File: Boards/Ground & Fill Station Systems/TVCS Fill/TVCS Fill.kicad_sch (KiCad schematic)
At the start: 111 parts, among them IC1 NSVT30010MXV6T1G, IC2 NSVT30010MXV6T1G, IC3 ADS1115IRUGR, J1 Conn_01x01_Socket, J10 Conn_01x01_Socket, J11 Conn_01x01_Socket, J12 Conn_01x01_Socket, J13 1190298, J14 1190298, J15 Conn_01x01_Socket, J17 XT30UPB-M, J18 Conn_01x01_Socket, J19 Conn_01x01_Socket, J2 1190297, J3 XT30UPB-M, J4 XT30UPB-M, J5 1190298, J6 XT30UPB-M, J8 Conn_01x01_Socket, J9 Conn_01x01_Socket, Q1 2N7002H6327XTSA2, U1 MAX31856MUD+T, U10 MAX31856MUD+T, U11 IRLZ44NPBF, U12 IRLZ44NPBF, U13 LM61460AASQRJRRQ1, U16 IRLZ44NPBF, U17 MAX485CSA+T, U3 MAX31856MUD+T, U4 PCA9306DP_118, U5 MCP9808T-E/MC, U9 LM61460AASQRJRRQ1

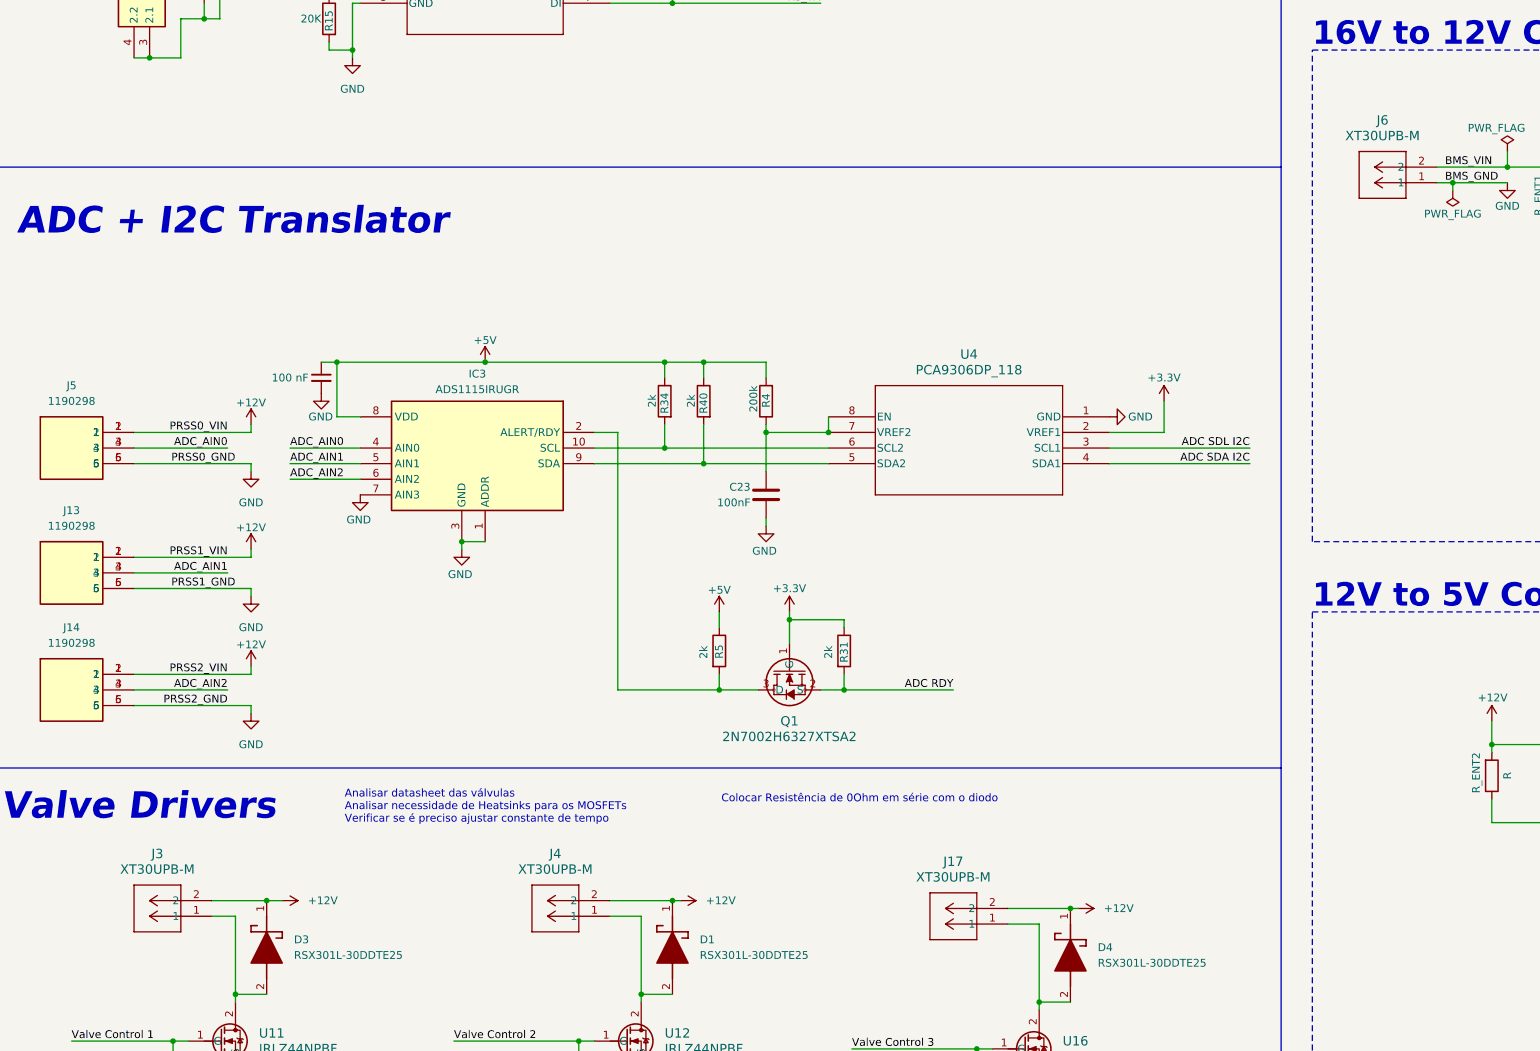
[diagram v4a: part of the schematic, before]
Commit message: XT30 to XT60
Connectores atualizados em toda as TVCS
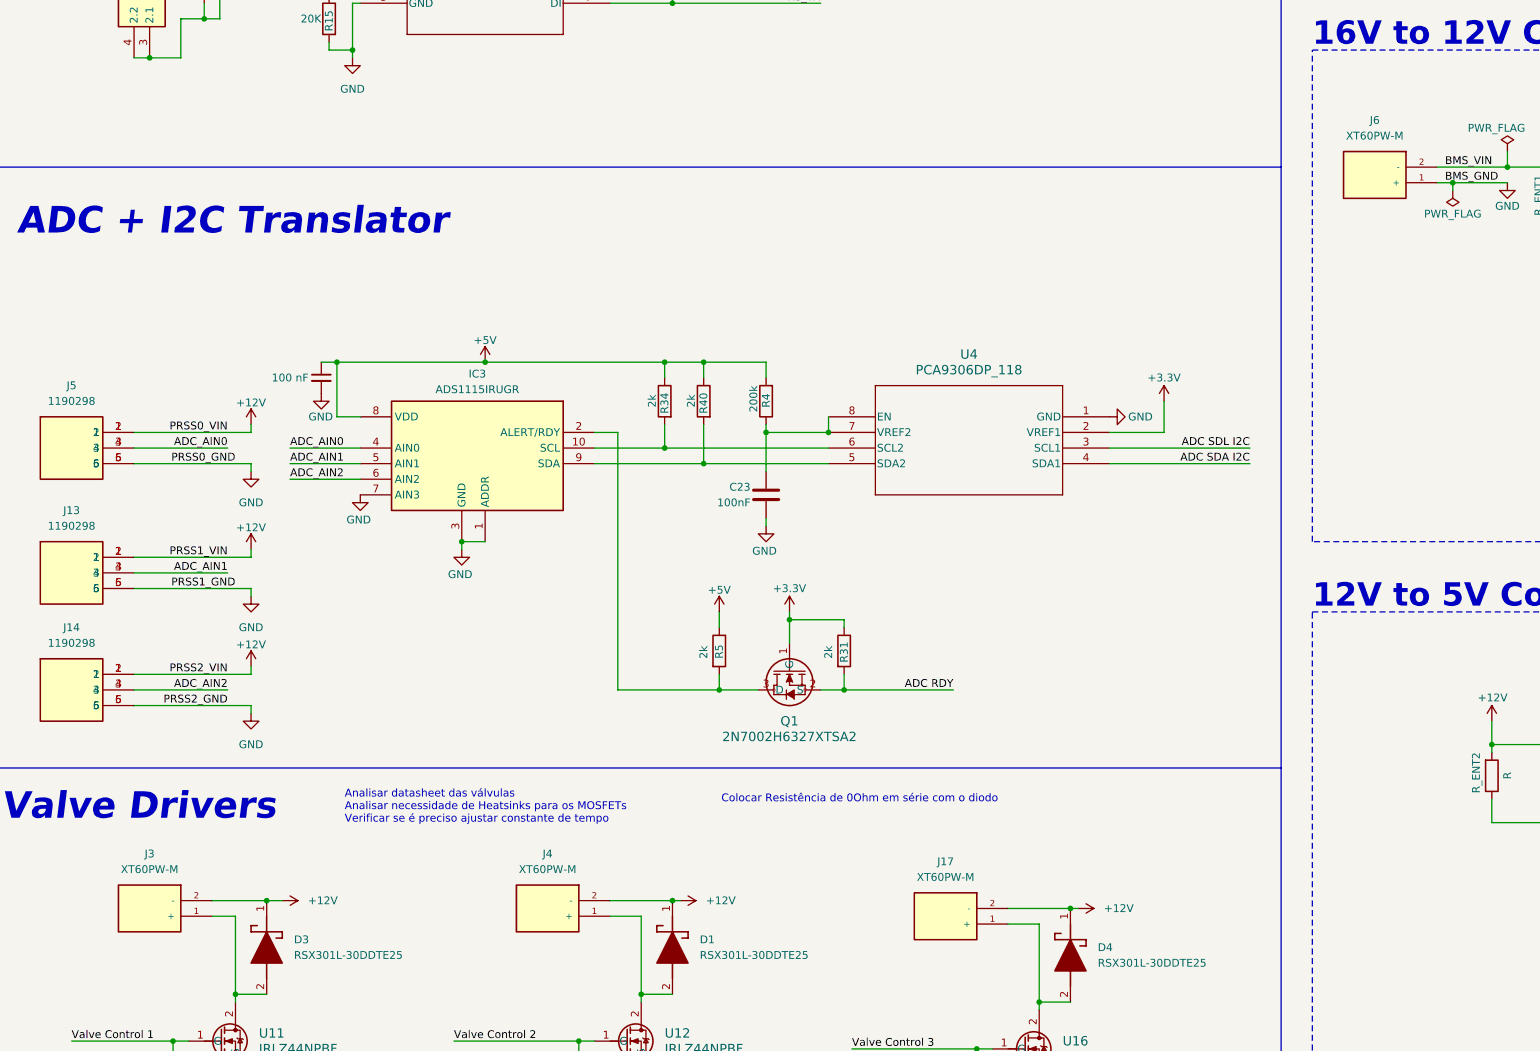
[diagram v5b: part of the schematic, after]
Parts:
- removed J17, J3, J4, J6: XT30UPB-M, CONN_XT30UPB-M_AMA, symbol AMASS_XT30UPB-M:XT30UPB-M
- added J17, J3, J4, J6: XT60PW-M, Conn XT60PW-M:AMASS_XT60PW-M, symbol XT60PW-M:XT60PW-M
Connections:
- net +12V: now also J17.2 (-), J3.2 (-), J4.2 (-)
- net +16V: now also J6.2 (-)
- net GND: now also J6.1 (+)
- net at D1.2 (A), U12.2: now also J4.1 (+)
- net at D3.2 (A), U11.2: now also J3.1 (+)
- net at D4.2 (A), U16.2: now also J17.1 (+)

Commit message: Final DCDC design and update part1 COMM board
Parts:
- removed C_FF1, C_FF2, C_OUT1, C_OUT2: C, Capacitor_0402:Capacitor_0402, symbol Device:C
- removed L3: L, Inductor_SMD:L_Neosid_SM-PIC0512H, symbol Device:L
- removed R_FF2, R_pull1, R_pull2: R, RES_0402:RES_0402, symbol Device:R
- removed U13: LM61460AASQRJRRQ1, VQFN-HR14_RJR_TEX, symbol DCDC_LM61460:LM61460AASQRJRRQ1
- added C_BIAS1, C_OUT3: 1u, Capacitor_0402:Capacitor_0402, symbol Device:C_Small
- added C_FF1: 22p, Capacitor_0402:Capacitor_0402, symbol Device:C_Small
- added C_IN1, C_IN2, C_IN3, C_IN4: 4.7u, Capacitor_0402:Capacitor_0402, symbol Device:C_Small
- added C_OUT1, C_OUT2, C_OUT5, C_OUT7: 22u, Capacitor_0402:Capacitor_0402, symbol Device:C_Small
- added C_OUT10, C_OUT4, C_OUT6, C_OUT8: 10u, Capacitor_0402:Capacitor_0402, symbol Device:C_Small
- added C_OUT11: 100u, Capacitor_0402:Capacitor_0402, symbol Device:C_Small
- added C_OUT9: 560u, Capacitor_0402:Capacitor_0402, symbol Device:C_Small
- added L2: 10u, Inductor_SMD:L_Neosid_SM-PIC0512H, symbol Device:L
- added R_BIAS1: 10, RES_0402:RES_0402, symbol Device:R
- added R_BT1: 100, RES_0402:RES_0402, symbol Device:R
- added R_BT2: 50, RES_0402:RES_0402, symbol Device:R
- added R_ENB1: 35k, RES_0402:RES_0402, symbol Device:R
- added R_ENB2: 100k, RES_0402:RES_0402, symbol Device:R
- added U8: LM61460AASQRJRRQ1, VQFN-HR14_RJR_TEX, symbol DCDC_LM61460:LM61460AASQRJRRQ1
- C_BT1, C_BT2, C_IN_HFI1, C_IN_HFI2, C_IN_HFI3, C_IN_HFI4: value C -> 100n
- C_IN-BLK1, C_IN-BLK2: value C -> 10u
- C_VCC1, C_VCC2: value C -> 1u
- L1: value L -> 15u
- R_ENT1: value R -> 400k
- R_ENT2: value R -> 1.15M
- R_FBB1: value R -> 24k9
- R_FBB2: value R -> 9k09
- R_FF1: value R -> 1k
- R_PG1, R_PG2: value R -> 100K
- R_RT1, R_RT2: value R -> 33k2
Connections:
- net +12V: now also R_FBT2.1, R_PG2.2, C_OUT10.1, C_OUT11.1, C_OUT3.1, C_OUT4.1, C_OUT6.1, C_OUT8.1, L2.2; no longer C_IN-BLK2.1, C_IN_HFI3.1, C_IN_HFI4.1, R_ENT2.2, R_FBT1.1, R_FF1.1, R_PG1.2, U9.12 (VIN2), U9.8 (VIN1)
- net +16V: now also C_IN-BLK2.1, C_IN_HFI3.1, C_IN_HFI4.1, R_ENT2.2, U9.12 (VIN2), U9.8 (VIN1), C_IN1.1, C_IN2.1, C_IN3.1, C_IN4.1, U8.12 (VIN2), U8.8 (VIN1)
- net +5V: no longer L1.2, R_FBT2.1, R_PG2.2, U9.1 (BIAS)
- net DC.DC1 PGOOD: now also C_VCC2.1, R_PG2.1, U9.2 (VCC), U9.5 (PGOOD); no longer R_PG1.1
- net DC.DC2 PGOOD: now also C_VCC1.1, R_PG1.1, U8.2 (VCC), U8.5 (PGOOD); no longer R_PG2.1, U9.5 (PGOOD)
- net GND: now also R_FBB1.2, R_FBB2.2, U9.1 (BIAS), C_BIAS1.2, C_IN1.2, C_IN2.2, C_IN3.2, C_IN4.2, C_OUT1.2, C_OUT10.2, C_OUT11.2, C_OUT2.2, C_OUT3.2, C_OUT4.2, C_OUT5.2, C_OUT6.2, C_OUT7.2, C_OUT8.2, C_OUT9.2, R_ENB1.1, R_ENB2.1, U8.11 (PGND2), U8.3 (AGND), U8.9 (PGND1); no longer R_FBB1.1, R_FBB2.1, R_FBT1.2, R_FBT2.2
- net at R_FF1.2: now also C_FF1.1
- net at C_BT1.1: now also L1.1, U8.10 (SW)
- net at C_BT1.2: now also R_BT1.1, U8.14 (CBOOT)
- net at R_RT1.2: now also U8.6 (RT)
- net at R_ENT1.1: now also R_ENB1.2, U8.7 (EN/SYNC)
- net at C_BT2.1, U9.10 (SW): now also L2.1; no longer L1.1
- net at C_BT2.2, U9.14 (CBOOT): now also R_BT2.1; no longer U9.13 (RBOOT)
- net at R_ENT2.1, U9.7 (EN/SYNC): now also R_ENB2.2
- net at U9.4 (FB): now also R_FBB2.1, R_FBT2.2; no longer R_FBB2.2
- new net: R_BT2.2, U9.13 (RBOOT)
- new net: R_BT1.2, U8.13 (RBOOT)
- new net: C_FF1.2, R_FBB1.1, R_FBT1.2, U8.4 (FB)
- new net: C_BIAS1.1, R_BIAS1.1, U8.1 (BIAS)
- new net 5V REG: C_OUT1.1, C_OUT2.1, C_OUT5.1, C_OUT7.1, C_OUT9.1, L1.2, R_BIAS1.2, R_FBT1.1, R_FF1.1, R_PG1.2
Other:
- note added: "16V to 5V Converter"
- note added: "C_IN-BLK1 and C_OUT8 are electrolytic polarized capacitors! All others are ceramic X7R capacitors with appropriate voltage ratings."
- note added: "C_IN-BLK2 and C_OUT11 are electrolytic polarized capacitors! All others are ceramic X7R capacitors with appropriate voltage ratings."
- note added: "DC.DC1 VCC coloca PGOOD a 3.3V"
- note added: "DC.DC2 VCC coloca PGOOD a 3.3V"
- note added: "Testar no LTSPICE a Bidirecionalidade!"
- note removed: "12V to 5V Converter"
- note removed: "Esta linha tem de estar a 3V3 para ligar ao RP2040!"
- moved on the sheet: C23, CR2, CR3, CR4, CR5, D1, D3, D4, IC1, IC2, IC3, J1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

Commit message: Tu viste o q eu fiz
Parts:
- removed C10: 10nF, Capacitor_0402:Capacitor_0402, symbol Device:C
- removed C17, C18, C20: 10nF, Capacitor_0402:Capacitor_0402, symbol Device:C_Small
- removed C19: 100nF, Capacitor_0402:Capacitor_0402, symbol Device:C_Small
- removed J1, J10, J11, J12, J8, J9: Conn_01x01_Socket, Button_Switch_THT:SW_Lever_1P2T_NKK_GW12LxH, symbol Connector:Conn_01x01_Socket
- removed J6: XT60PW-M, Conn XT60PW-M:AMASS_XT60PW-M, symbol XT60PW-M:XT60PW-M
- removed U10: MAX31856MUD+T, 21-0066J_14_MXM, symbol MAX31856MUD-T:MAX31856MUD+T
- removed U17: MAX485CSA+T, 21-0041-3-M_90-0096-8L_MXM, symbol RS_Transceiver:MAX485CSA+T
- removed U5: MCP9808T-E/MC, DFN8_2x3MC_MCH, symbol MCP9808:MCP9808T-E_MC
- removed U8, U9: LM61460AASQRJRRQ1, VQFN-HR14_RJR_TEX, symbol DCDC_LM61460:LM61460AASQRJRRQ1
- added C10, C12, C13, C5: 10nF, Capacitor-0402:Capacitor_0402, symbol Device:C_Small
- added C14: 10nF, Capacitor-0402:Capacitor_0402, symbol Device:C
- added J1, J6: 1190298, LPT Conn 3 Entradas:1190298, symbol 1190298:1190298
- added J8: XT60PW-M, Button_Switch_THT:SW_Lever_1P2T_NKK_GW12LxH, symbol XT60PW-M:XT60PW-M
- added U10: LM61460AASQRJRRQ1, Thermocouple:21-0066J_14_MXM, symbol DCDC_LM61460:LM61460AASQRJRRQ1
- added U13: LM61460AASQRJRRQ1, DCDC_LM61460:VQFN-HR14_RJR_TEX, symbol DCDC_LM61460:LM61460AASQRJRRQ1
- added U5: MAX485CSA+T, MCP9808-TempSensor:DFN8_2x3MC_MCH, symbol RS_Transceiver:MAX485CSA+T
- added U8: MCP9808T-E/MC, DCDC_LM61460:VQFN-HR14_RJR_TEX, symbol MCP9808:MCP9808T-E_MC
- added U9: MAX31856MUD+T, DCDC_LM61460:VQFN-HR14_RJR_TEX, symbol MAX31856MUD-T:MAX31856MUD+T
- C1, C11, C2, C23, C4, C7, C8, C_BT1, C_BT2, C_FF1, C_IN_HFI1, C_IN_HFI2, C_IN_HFI3, C_IN_HFI4: footprint Capacitor_0402:Capacitor_0402 -> Capacitor-0402:Capacitor_0402
- C3, C9: value 10nF -> 100nF; footprint Capacitor_0402:Capacitor_0402 -> Capacitor-0402:Capacitor_0402
- C6: value 100nF -> 10nF; footprint Capacitor_0402:Capacitor_0402 -> Capacitor-0402:Capacitor_0402
- CR2, CR3, CR4, CR5: footprint LED_PLCC_VSMB -> LED-Green_VLMC3100-GS08:LED_PLCC_VSMB
- C_BIAS1, C_OUT3, C_VCC1, C_VCC2: footprint Capacitor_0402:Capacitor_0402 -> Capacitor-0603:Capacitor_0603
- C_IN-BLK1, C_IN-BLK2: footprint Capacitor_0402:Capacitor_0402 -> Capacitor-4mm:Capacitor_4mm
- C_IN1, C_IN2, C_IN3, C_IN4: footprint Capacitor_0402:Capacitor_0402 -> Capacitor-1206:Capacitor_1206
- C_OUT1, C_OUT10, C_OUT2, C_OUT4, C_OUT5, C_OUT6, C_OUT7, C_OUT8: footprint Capacitor_0402:Capacitor_0402 -> Capacitor-0805:Capacitor_0805
- C_OUT11: footprint Capacitor_0402:Capacitor_0402 -> Capacitor-6mm:Capacitor_6mm
- C_OUT9: footprint Capacitor_0402:Capacitor_0402 -> Capacitor-8mm:Capacitor_8mm
- D1, D3, D4: footprint DIOM5026X220N -> Diode-Schottky_RSX301L:DIOM5026X220N
- IC1, IC2: footprint SOTFL50P160X60-6N -> 2 PNP:SOTFL50P160X60-6N
- IC3: footprint ADS1115IRUGR -> ADS1115:ADS1115IRUGR
- J2: footprint 1190297 -> LPT Conn 2 Entradas:1190297
- L1: footprint Inductor_SMD:L_Neosid_SM-PIC0512H -> Inductor-10.1x10:Inductor_10.1x10
- L2: footprint Inductor_SMD:L_Neosid_SM-PIC0512H -> Inductor-11.5x10:Inductor_11.5x10
- Q1: footprint PG-SOT23-3-5_INF_MIN -> NMOS_2N7002:PG-SOT23-3-5_INF_MIN
- R1, R14, R17, R2, R31, R34, R37, R4, R40, R5, R6, R7, R_BIAS1, R_BT1, R_BT2, R_ENB1, R_FF1: footprint RES_0402:RES_0402 -> Resistor-0402:RES_0402
- R10, R9: value 10K -> 20K; footprint RES_0402:RES_0402 -> Resistor-0402:RES_0402
- R11: value 20K -> 10K; footprint RES_0402:RES_0402 -> Resistor-0402:RES_0402
- R12, R13: value 2k -> 10K; footprint RES_0402:RES_0402 -> Resistor-0402:RES_0402
- R15: value 20K -> 2k; footprint RES_0402:RES_0402 -> Resistor-0402:RES_0402
- R16: value 120 -> 100; footprint RES_0402:RES_0402 -> Resistor-0402:RES_0402
- R18: value 1k -> 100; footprint RC0402N_VIS:RC0402N_VIS -> Resistor-0402:RES_0402
- R19, R20: value 1k -> 2k; footprint RC0402N_VIS:RC0402N_VIS -> Resistor-0402:RES_0402
- R21: footprint RC0402N_VIS:RC0402N_VIS -> Resistor-0402:RES_0402
- R27: value 2k -> 1k; footprint RES_0402:RES_0402 -> Resistor-0402:RES_0402
- R28, R32: value 100 -> 1k; footprint RES_0402:RES_0402 -> Resistor-0402:RES_0402
- R8: value 10K -> 120; footprint RES_0402:RES_0402 -> Resistor-0402:RES_0402
- R_ENB2, R_ENT2, R_FBB1, R_FBB2, R_FBT1, R_FBT2, R_PG1, R_PG2, R_RT1, R_RT2: footprint RES_0402:RES_0402 -> Resistor-0603:RES_0603
- R_ENT1: footprint RES_0402:RES_0402 -> Resistor-0805:RES_0805
- U1, U3: footprint 21-0066J_14_MXM -> Thermocouple:21-0066J_14_MXM
- U11, U12, U16: footprint PG-TO220-3_INF -> NMOS IRLZ44:PG-TO220-3_INF
- U4: footprint TSSOP8_SOT505-1_NXP -> I2C Voltage Translator:TSSOP8_SOT505-1_NXP
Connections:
- net +16V: now also J8.2 (-), U10.12 (VIN2), U10.8 (VIN1), U13.12 (VIN2), U13.8 (VIN1)
- net +3.3V: now also C6.2, C7.2, R11.1, R13.2, R15.1, R19.1, R20.1, C12.2, C13.2, C14.1, C5.2, U8.8 (VDD), U9.5 (AVDD), U9.8 (DVDD); no longer C3.2, C4.2, C9.2, R10.1, R13.1, R27.1, R8.2, R9.1
- net +5V: now also R9.1, U5.8 (VCC); no longer R11.1
- net DC.DC1 PGOOD: now also U13.2 (VCC), U13.5 (PGOOD)
- net DC.DC2 PGOOD: now also U10.2 (VCC), U10.5 (PGOOD)
- net GND: now also C4.2, C6.1, C7.1, R10.2, C10.2, C12.1, C13.1, C14.2, C5.1, J8.1 (+), U10.11 (PGND2), U10.3 (AGND), U10.9 (PGND1), U13.1 (BIAS), U13.11 (PGND2), U13.3 (AGND), U13.9 (PGND1), U5.5 (GND), U8.4 (GND), U8.5 (A2), U8.6 (A1), U8.7 (A0), U8.9 (EPAD), U9.1 (AGND), U9.14 (DGND); no longer C3.1, C4.1, C7.2, C9.1, R15.2
- net RS_ENABLE: now also R12.2, U5.2 (*RE), U5.3 (DE); no longer R9.2
- net RS_RX: now also R11.2, U5.1 (RO); no longer R10.2
- net RS_TX: now also R13.1, U5.4 (DI); no longer R8.1
- net SPI_MISO: now also U9.11 (SDO)
- net SPI_MOSI: now also U9.12 (SDI)
- net SPI_SCK: now also U9.10 (SCK)
- net TEMP ALERT: now also R15.2, U8.3 (ALERT); no longer R27.2
- net TEMP SDA I2C: now also R20.2, U8.1 (SDA); no longer R12.2
- net TEMP SDL I2C: now also R19.2, U8.2 (SCL); no longer R13.2
- net THERMO1 T+: now also R1.2, J1.1, J1.2; no longer R28.2
- net THERMO1 T-: now also R2.2, U1.2 (BIAS), J1.3, J1.4; no longer R32.2
- net THERMO1_~{CS}: now also U1.9 (~{CS})
- net THERMO1_~{DRDY}: now also U1.7 (~{DRDY})
- net THERMO1_~{FAULT}: now also U1.13 (~{FAULT})
- net THERMO2 T+: now also R6.2, J1.5, J1.6; no longer R1.2
- net THERMO2 T-: now also R7.2, U3.2 (BIAS), J6.1, J6.2; no longer R2.2, U1.2 (BIAS)
- net THERMO2_~{CS}: now also U3.9 (~{CS}); no longer U1.9 (~{CS})
- net THERMO2_~{DRDY}: now also U3.7 (~{DRDY}); no longer U1.7 (~{DRDY})
- net THERMO2_~{FAULT}: now also U3.13 (~{FAULT}); no longer U1.13 (~{FAULT})
- net THERMO3 T+: now also R16.2, J6.3, J6.4; no longer R6.2
- net THERMO3 T-: now also R18.2, J6.5, J6.6, U9.2 (BIAS); no longer R7.2, U3.2 (BIAS)
- net THERMO3_~{CS}: now also U9.9 (~{CS}); no longer U3.9 (~{CS})
- net THERMO3_~{DRDY}: now also U9.7 (~{DRDY}); no longer U3.7 (~{DRDY})
- net THERMO3_~{FAULT}: now also U9.13 (~{FAULT}); no longer U3.13 (~{FAULT})
- net at R6.1, U3.4 (T+): now also C3.1; no longer C6.1
- net at IC1.4 (E1): now also R21.1; no longer R18.1
- net at CR2.1: now also R21.2; no longer R18.2
- net at J2.3 (2.1), J2.4 (2.2): now also R8.2, R9.2, U5.6 (A); no longer R11.2, R16.2
- net at J2.1 (1.1), J2.2 (1.2): now also R10.1, R8.1, U5.7 (B); no longer R15.1, R16.1
- net at R_ENB2.2, R_ENT2.1: now also U13.7 (EN/SYNC)
- net at IC1.1 (E2): now also R27.1; no longer R19.1
- net at CR3.1: now also R27.2; no longer R19.2
- net at C_BT2.2, R_BT2.1: now also U13.14 (CBOOT)
- net at R_BT2.2: now also U13.13 (RBOOT)
- net at R_RT1.2: now also U10.6 (RT)
- net at R32.1: now also IC2.1 (E2)
- net at CR5.1: now also R32.2; no longer R21.2
- net at IC2.4 (E1): now also R28.1; no longer R20.1
- net at CR4.1: now also R28.2; no longer R20.2
- net at C_BT1.2, R_BT1.1: now also U10.14 (CBOOT)
- net at R_BT1.2: now also U10.13 (RBOOT)
- net at C_FF1.2, R_FBB1.1, R_FBT1.2: now also U10.4 (FB)
- net at C_BT2.1, L2.1: now also U13.10 (SW)
- net at C_BT1.1, L1.1: now also U10.10 (SW)
- net at R7.1, U3.3 (T-): now also C3.2, C4.1; no longer C6.2, C7.1
- net at R_ENB1.2, R_ENT1.1: now also U10.7 (EN/SYNC)
- net at C_BIAS1.1, R_BIAS1.1: now also U10.1 (BIAS)
- net at R_FBB2.1, R_FBT2.2: now also U13.4 (FB)
- net at R_RT2.2: now also U13.6 (RT)
- new net: C10.1, C9.2, R18.1, U9.3 (T-)
- new net: C9.1, R16.1, U9.4 (T+)
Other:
- moved on the sheet: C23, D1, D3, D4, IC3, J13, J14, J17, J3, J4, J5, Q1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
